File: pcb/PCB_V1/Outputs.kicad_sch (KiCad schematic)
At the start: 18 parts, among them J501 FAN1 / WAGO 2601, J511 FAN2 / WAGO 2601, J521 PUMP + / switched -, Q501 AO3400A, Q511 AO3400A, Q521 AO3400A

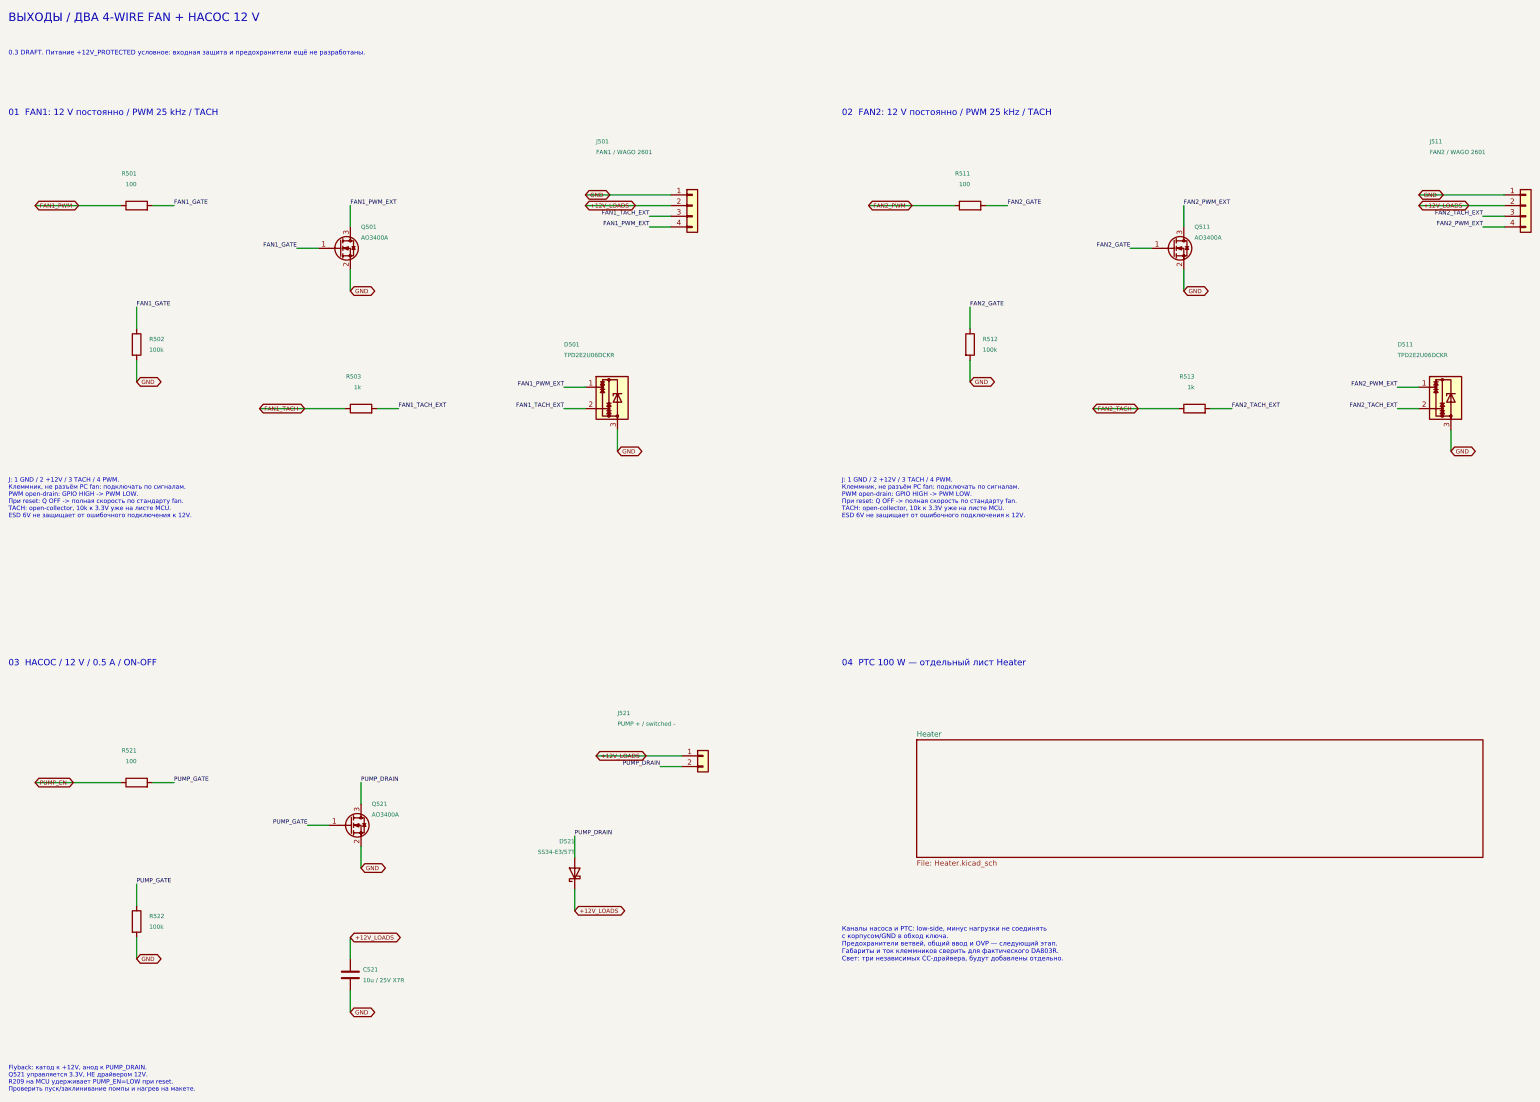
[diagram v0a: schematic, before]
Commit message: pcb: add individual branch fuses and qualified terminal geometry
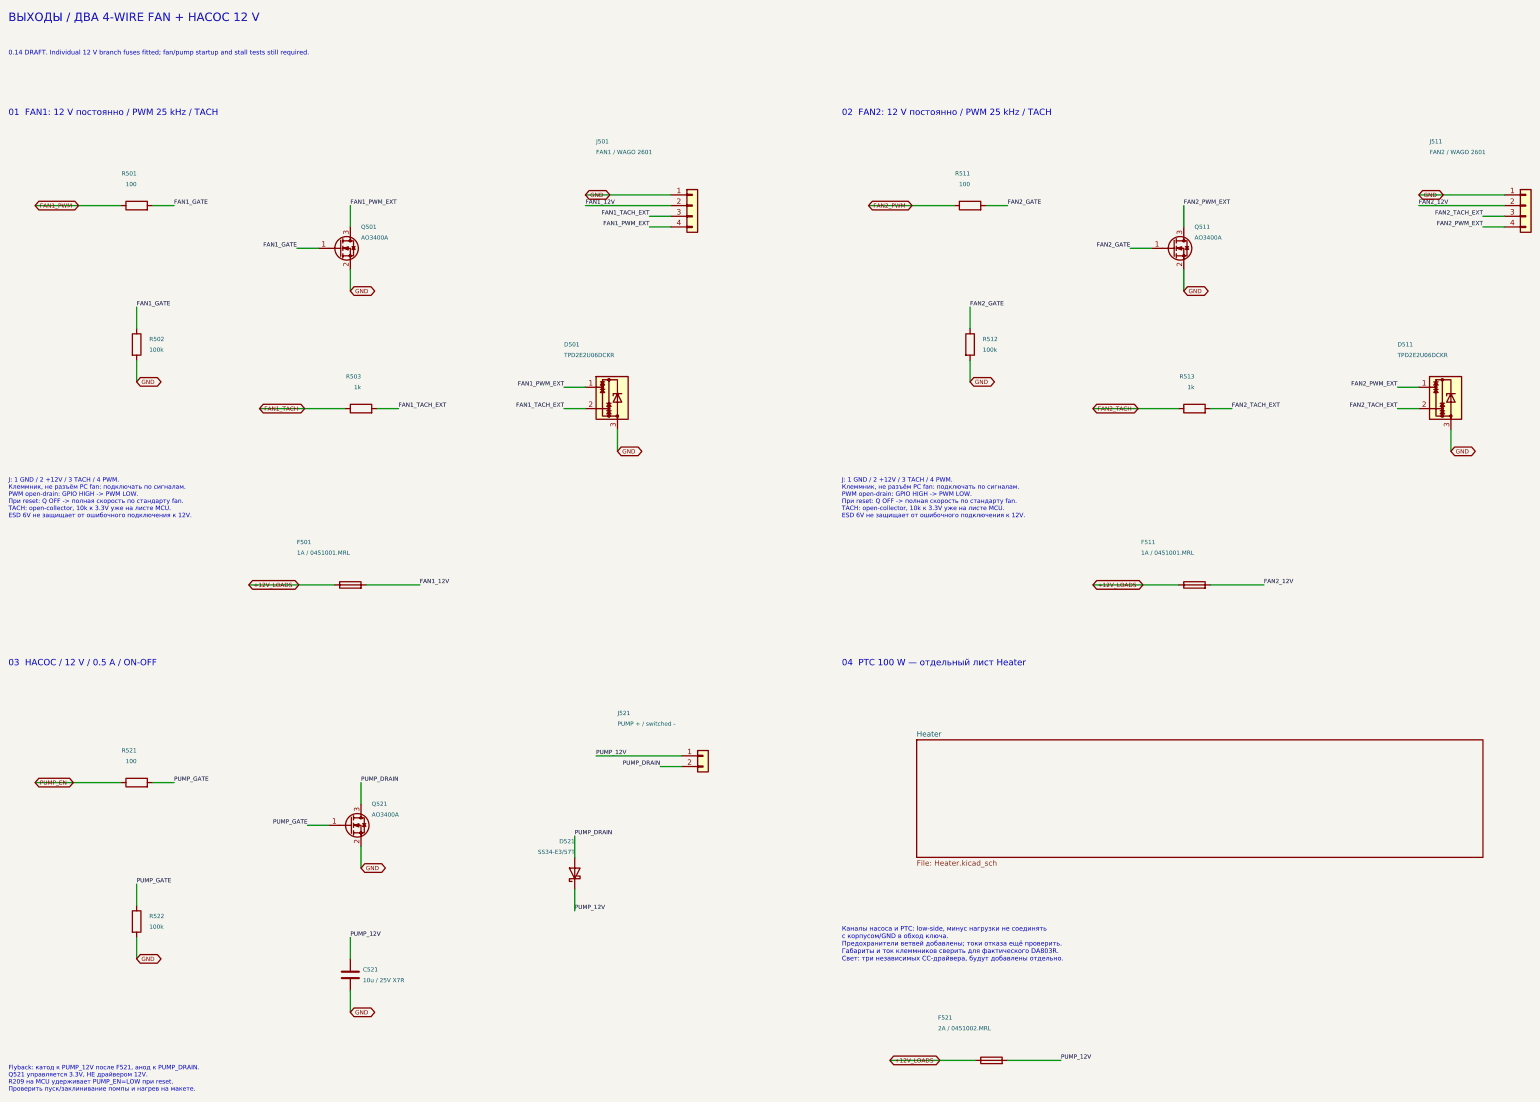
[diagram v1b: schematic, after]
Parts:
- added F501, F511: 1A / 0451001.MRL, GrowBox:Fuse_Littelfuse_451, symbol Device:Fuse
- added F521: 2A / 0451002.MRL, GrowBox:Fuse_Littelfuse_451, symbol Device:Fuse
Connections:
- net +12V_LOADS: now also F501.1, F511.1, F521.1; no longer C521.1, D521.1 (K), J501.2 (Pin_2), J511.2 (Pin_2), J521.1 (Pin_1)
- new net FAN1_12V: F501.2, J501.2 (Pin_2)
- new net FAN2_12V: F511.2, J511.2 (Pin_2)
- new net PUMP_12V: C521.1, D521.1 (K), F521.2, J521.1 (Pin_1)
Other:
- note added: "0.14 DRAFT. Individual 12 V branch fuses fitted; fan/pump startup and stall tests still required."
- note added: "Flyback: катод к PUMP_12V после F521, анод к PUMP_DRAIN. Q521 управляется 3.3V, НЕ драйвером 12V. R209 на MCU удерживает PUMP_EN=LOW при reset. Проверить пуск/заклинивание помпы и нагрев на макете."
- note added: "Каналы насоса и PTC: low-side, минус нагрузки не соединять с корпусом/GND в обход ключа. Предохранители ветвей добавлены; токи отказа ещё проверить. Габариты и ток клеммников сверить для фактического DA803R. Свет: три независимых CC-драйвера, будут добавлены отдельно."
- note removed: "0.3 DRAFT. Питание +12V_PROTECTED условное: входная защита и предохранители ещё не разработаны."
- note removed: "Flyback: катод к +12V, анод к PUMP_DRAIN. Q521 управляется 3.3V, НЕ драйвером 12V. R209 на MCU удерживает PUMP_EN=LOW при reset. Проверить пуск/заклинивание помпы и нагрев на макете."
- note removed: "Каналы насоса и PTC: low-side, минус нагрузки не соединять с корпусом/GND в обход ключа. Предохранители ветвей, общий ввод и OVP — следующий этап. Габариты и ток клеммников сверить для фактического DA803R. Свет: три независимых CC-драйвера, будут добавлены отдельно."
